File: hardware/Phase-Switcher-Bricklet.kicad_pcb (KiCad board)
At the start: 2 copper layers, 60 x 60 mm, 42 parts, among them CN1 HC-GH-7PWTKK, P1 WJ124-3.81-2P, P2 WJ124-3.81-6P, P3 WJ124-3.81-6P, U1 XMC1302-Q024X0032-AB, U2 AQY282SX, U3 AQH3213A, U4 HCPL2731S, U5 AQH3213A, U6 HCPL2731S

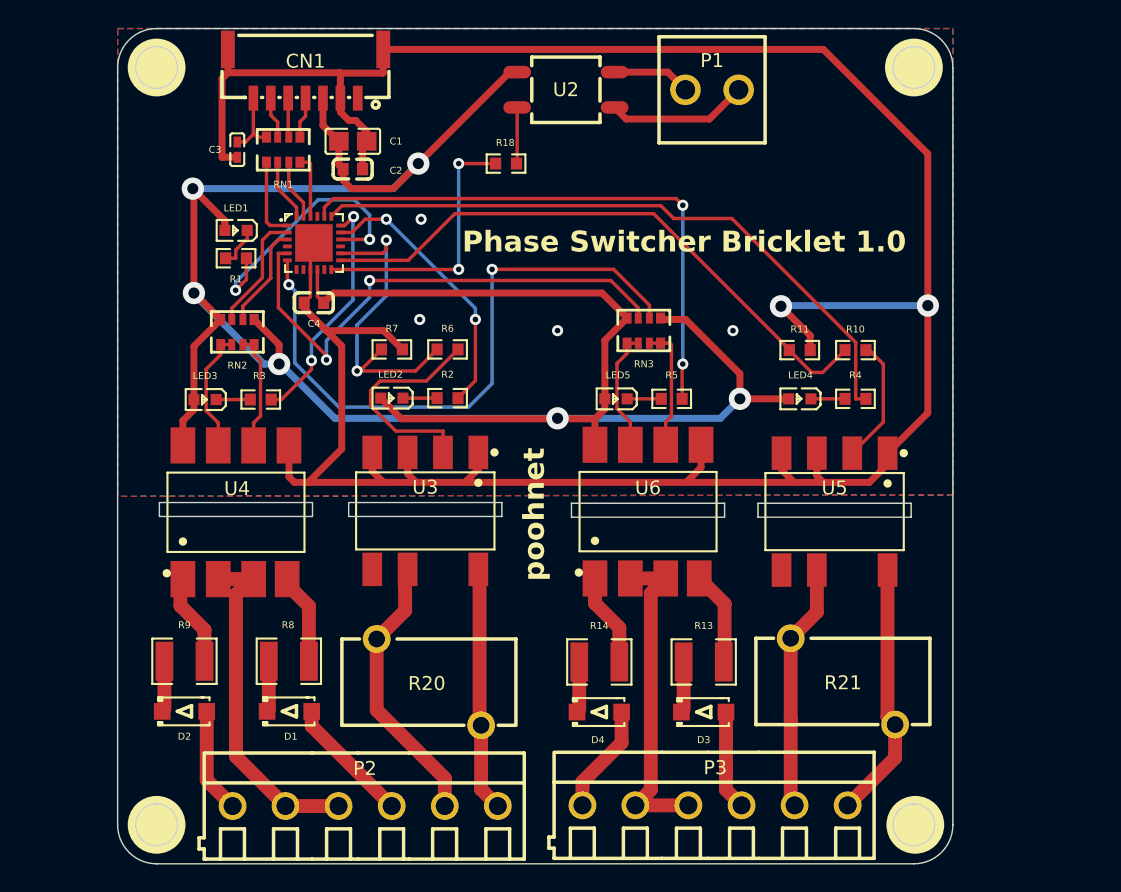
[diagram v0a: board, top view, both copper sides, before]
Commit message: Phase-Switcher-Bricklet: Rev. 1.1
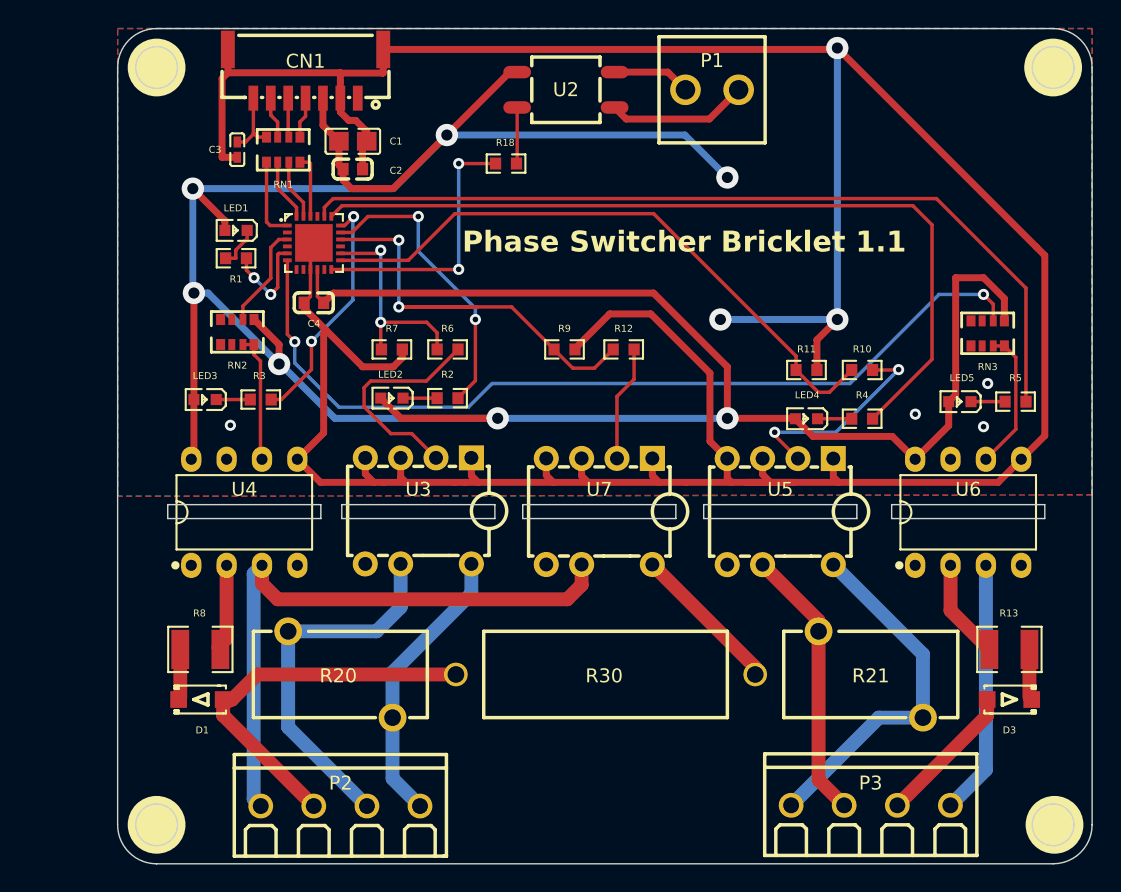
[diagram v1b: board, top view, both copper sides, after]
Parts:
- removed D2, D4: 1N4007, easyeda2kicad:SOD-123FL_L2.8-W1.8-LS3.7-RD
- removed R14: CR1210F249KP05, easyeda2kicad:R1210
- added R12: 150, easyeda2kicad:R0603, F.Cu at (92.8, 60.6)
- added R30: RSF5SSJR-73-4K7, easyeda2kicad:RES-TH_BD6.5-L17.5-P21.50-D0.6, F.Cu at (91.5, 84.0)
- added U7: AQH2213, easyeda2kicad:DIP-8_7P-L9.7-W6.4-P2.54-LS7.6-BL-PE7, F.Cu at (91.0, 72.3)
- P2, P3: value WJ124-3.81-6P -> WJ124-3.81-4P; footprint easyeda2kicad:CONN-TH_6P-P3.81_WJ124-3.81-6P -> easyeda2kicad:CONN-TH_4P-P3.81_KF124-3.81-4P
- R9: value CR1210F249KP05 -> 1K; footprint easyeda2kicad:R1210 -> easyeda2kicad:R0603
- U3, U5: value AQH3213A -> AQH2213; footprint easyeda2kicad:SMD-8_7P-L9.8-W6.4-P2.54-BL-PE7 -> easyeda2kicad:DIP-8_7P-L9.7-W6.4-P2.54-LS7.6-BL-PE7
- U4, U6: value HCPL2731S -> 6N139M; footprint easyeda2kicad:SMD-8_L9.8-W6.6-P2.54-LS10.3-BL -> easyeda2kicad:DIP-8_L9.4-W6.4-P2.54-LS9.1-BL
- moved R9 35.3 mm to (88.5, 60.6), turned to 0 degrees
- moved LED5 24.7 mm to (116.9, 64.4)
- moved R5 24.7 mm to (120.9, 64.4)
- moved RN3 24.7 mm to (118.9, 59.5)
- moved U6 23.0 mm to (117.5, 72.3)
- moved D3 22.0 mm to (120.5, 85.8), turned to 180 degrees
- moved R13 22.0 mm to (120.5, 82.2), turned to 0 degrees
- moved P3 11.2 mm to (110.5, 93.4)
- moved R8 6.42 mm to (62.3, 82.2)
- moved D1 6.42 mm to (62.4, 85.8)
- moved R20 6.38 mm to (72.4, 84.0)
- moved U5 3.90 mm to (104.0, 72.3)
- moved R21 2.06 mm to (110.5, 84.0)
- moved P2 1.78 mm to (72.4, 93.5)
- moved LED4 1.51 mm to (105.9, 65.6)
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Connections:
- net AC1-1 renamed AC1
- net AC2-1 renamed AC2
- P2 pad 4: Net-(U4-VF1-) -> Net-(U4-VF-)
- P3 pad 1: Net-(P3-Pad1) -> Net-(U6-VF-)
- P3 pad 2: Net-(P3-Pad2) -> Net-(D3-A)
- P3 pad 3: Net-(D3-A) -> Net-(P3-Pad3)
- P3 pad 4: Net-(U6-VF1-) -> Net-(P3-Pad4)
- R13 pad 1: Net-(U6-VF2+) -> Net-(U6-VF+)
- R21 pad 1: Net-(P3-Pad2) -> Net-(P3-Pad3)
- R21 pad 2: Net-(P3-Pad1) -> Net-(P3-Pad4)
- R8 pad 1: Net-(U4-VF2+) -> Net-(U4-VF+)
- R9 pad 1: Net-(U4-VF1+) -> RCD
- R9 pad 2: Net-(D2-K) -> GND
- RN2 pad 1: Net-(U4-VO1) -> unconnected-(RN2-Pad1)
- RN2 pad 2: Net-(U4-VO1) -> unconnected-(RN2-Pad2)
- RN2 pad 7: AC1-2 -> unconnected-(RN2-Pad7)
- RN2 pad 8: 3V3 -> unconnected-(RN2-Pad8)
- RN3 pad 1: Net-(U6-VO1) -> unconnected-(RN3-Pad1)
- RN3 pad 2: Net-(U6-VO1) -> unconnected-(RN3-Pad2)
- RN3 pad 7: AC2-2 -> unconnected-(RN3-Pad7)
- RN3 pad 8: 3V3 -> unconnected-(RN3-Pad8)
- U1 pad 16: LED1 -> RCD
- U1 pad 2: AC1-2 -> unconnected-(U1-P2.1-Pad2)
- U1 pad 5: AC2-2 -> LED1
- U4 pad 1: Net-(U4-VF1+) -> unconnected-(U4-N/C-Pad1)
- U4 pad 2: Net-(U4-VF1-) -> Net-(U4-VF+)
- U4 pad 3: Net-(U4-VF1-) -> Net-(U4-VF-)
- U4 pad 4: Net-(U4-VF2+) -> unconnected-(U4-N/C-Pad4)
- U4 pad 7: Net-(U4-VO1) -> unconnected-(U4-VB-Pad7)
- U5 pad 6: Net-(P3-Pad2) -> Net-(P3-Pad3)
- U5 pad 8: Net-(P3-Pad1) -> Net-(P3-Pad4)
- U6 pad 1: Net-(U6-VF1+) -> unconnected-(U6-N/C-Pad1)
- U6 pad 2: Net-(U6-VF1-) -> Net-(U6-VF+)
- U6 pad 3: Net-(U6-VF1-) -> Net-(U6-VF-)
- U6 pad 4: Net-(U6-VF2+) -> unconnected-(U6-N/C-Pad4)
- U6 pad 7: Net-(U6-VO1) -> unconnected-(U6-VB-Pad7)
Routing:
- net GND: track 198.1 -> 250.1 mm, vias 6 -> 7
- net Net-(U4-VF-): track 0.00 -> 44.4 mm
- net 3V3: track 175.9 -> 215.3 mm, vias 6 -> 7
- net AC2-2: track 37.5 -> 0.00 mm, vias 2 -> 0
- net RCD: track 0.00 -> 32.4 mm, vias 0 -> 2
- net Net-(U4-VF1-): track 25.9 -> 0.00 mm
- net Net-(P3-Pad4): track 0.00 -> 25.7 mm
- net Net-(P3-Pad2): track 23.7 -> 0.00 mm
- net Net-(U6-VF1-): track 23.6 -> 0.00 mm
- net LED5: track 40.8 -> 62.1 mm, vias 2 -> 0
- net Net-(P3-Pad3): track 0.00 -> 19.7 mm
- net Net-(D1-A): track 9.18 -> 27.8 mm
- net AC2: track 45.3 -> 63.9 mm
- net Net-(P3-Pad1): track 18.5 -> 0.00 mm
- net Net-(U6-VF-): track 0.00 -> 18.3 mm
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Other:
- board size 60 x 60 mm -> 70 x 60 mm
- board text added: "Phase Switcher Bricklet 1.1"
- board text removed: "Phase Switcher Bricklet 1.0"
- board text removed: "poohnet"

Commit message: Phase-Switcher-Bricklet: Rev. 1.1a
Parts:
- removed RN3: 10K, easyeda2kicad:RES-ARRAY-SMD_0603-8P-L3.2-W1.6-BL
- added LED6: blue, easyeda2kicad:LED0603-RD, F.Cu at (102.2, 58.4)
- added R6: 1K, easyeda2kicad:R0603, F.Cu at (105.9, 58.4)
- U10: renamed from U3; value AQH2213 -> AQH2223
- U20: renamed from U5; value AQH2213 -> AQH2223
- U30: renamed from U7; value AQH2213 -> AQH2223
- moved RN2 26.5 mm to (91.4, 61.6)
- moved U40 25.5 mm to (104.1, 62.2)
- moved P40 20.8 mm to (114.9, 55.5)
- moved R40 20.3 mm to (96.5, 63.5)
- moved C1 17.8 mm to (82.5, 61.0)
- moved C2 17.8 mm to (82.5, 63.0)
- moved CN1 16.0 mm to (78.0, 54.6)
- moved R11 15.2 mm to (65.5, 64.8)
- moved R10 15.0 mm to (61.7, 64.8), turned to 180 degrees
- moved R2 14.9 mm to (65.5, 67.3)
- moved LED2 14.8 mm to (61.7, 67.3)
- moved U20 14.2 mm to (118.1, 74.0)
- moved U10 14.1 mm to (64.0, 74.0)
- moved RN1 13.7 mm to (71.1, 59.7), turned to 90 degrees
- moved LED3 13.7 mm to (76.0, 67.3)
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- renumbered D1 to D10, D3 to D20, P2 to P10, P3 to P20, P1 to P40, R7 to R10, R6 to R11, R20 to R12, R8 to R13, R11 to R20, R10 to R21, R21 to R22, R13 to R23, R9 to R30, R12 to R31, R30 to R32, R18 to R40, U4 to U11, U6 to U21, U2 to U40
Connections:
- net Net-(U4-VO) renamed AC1-1
- D10 pad 2: Net-(D1-A) -> Net-(D10-A)
- D20 pad 2: Net-(D3-A) -> Net-(D20-A)
- P10 pad 1: Net-(P2-Pad1) -> Net-(U11-VF-)
- P10 pad 2: Net-(P2-Pad2) -> Net-(D10-A)
- P10 pad 3: Net-(D1-A) -> Net-(P10-Pad3)
- P10 pad 4: Net-(U4-VF-) -> Net-(P10-Pad4)
- P20 pad 1: Net-(U6-VF-) -> Net-(P20-Pad1)
- P20 pad 2: Net-(D3-A) -> Net-(P20-Pad2)
- P20 pad 3: Net-(P3-Pad3) -> Net-(D20-A)
- P20 pad 4: Net-(P3-Pad4) -> Net-(U21-VF-)
- R12 pad 1: Net-(P2-Pad2) -> Net-(P10-Pad4)
- R12 pad 2: Net-(P2-Pad1) -> Net-(P10-Pad3)
- R22 pad 1: Net-(P3-Pad3) -> Net-(P20-Pad2)
- R22 pad 2: Net-(P3-Pad4) -> Net-(P20-Pad1)
- R32 pad 2: Net-(D1-A) -> Net-(D10-A)
- RN2 pad 1: unconnected-(RN2-Pad1) -> AC2-1
- RN2 pad 2: unconnected-(RN2-Pad2) -> AC2-1
- RN2 pad 7: unconnected-(RN2-Pad7) -> 3V3
- RN2 pad 8: unconnected-(RN2-Pad8) -> AC2
- U1 pad 11: unconnected-(U1-P1.3-Pad11) -> RCD
- U1 pad 16: RCD -> LED1
- U1 pad 21: unconnected-(U1-P0.12-Pad21) -> LED6
- U1 pad 5: LED1 -> unconnected-(U1-P2.7/P2.8-Pad5)
- U10 pad 6: Net-(P2-Pad2) -> Net-(P10-Pad4)
- U10 pad 8: Net-(P2-Pad1) -> Net-(P10-Pad3)
- U11 pad 3: Net-(U4-VF-) -> Net-(U11-VF-)
- U20 pad 6: Net-(P3-Pad3) -> Net-(P20-Pad2)
- U20 pad 8: Net-(P3-Pad4) -> Net-(P20-Pad1)
- U21 pad 3: Net-(U6-VF-) -> Net-(U21-VF-)
- U21 pad 6: Net-(U6-VO) -> AC2-1
- U30 pad 6: Net-(U4-VF-) -> Net-(U11-VF-)
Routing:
- net GND: track 250.1 -> 128.8 mm, vias 7 -> 8
- net 3V3: track 215.3 -> 112.2 mm, vias 7 -> 0
- net RCD: track 32.4 -> 96.7 mm
- net LED6: track 0.00 -> 46.3 mm, vias 0 -> 2
- net Net-(U4-VF-): track 44.4 -> 0.00 mm
- net Net-(U11-VF-): track 0.00 -> 40.0 mm
- net AC2: track 63.9 -> 31.1 mm
- net Net-(D1-A): track 27.8 -> 0.00 mm
- net Net-(P2-Pad2): track 27.1 -> 0.00 mm
- net Net-(P3-Pad4): track 25.7 -> 0.00 mm
- net AC1: track 7.43 -> 32.2 mm, vias 0 -> 2
- net Net-(P20-Pad1): track 0.00 -> 22.3 mm
- net Net-(P10-Pad4): track 0.00 -> 22.1 mm
- net Net-(P2-Pad1): track 21.4 -> 0.00 mm
- net Net-(P20-Pad2): track 0.00 -> 20.8 mm
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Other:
- board size 70 x 60 mm -> 70 x 46.4 mm
- board text added: "poohnet"

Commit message: Phase-Switcher-Bricklet: Rev. 1.2
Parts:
- removed P20: WJ124-3.81-4P, easyeda2kicad:CONN-TH_4P-P3.81_KF124-3.81-4P
- removed R30: 1K, easyeda2kicad:R0603
- removed R31: 150, easyeda2kicad:R0603
- removed R32: RSF5SSJR-73-4K7, easyeda2kicad:RES-TH_BD6.5-L17.5-P21.50-D0.6
- removed U30: AQH2223, easyeda2kicad:DIP-8_7P-L9.7-W6.4-P2.54-LS7.6-BL-PE7
- added P11: WJ124-3.81-2P, easyeda2kicad:CONN-TH_2P-P3.81_KF124-3.81-2P, F.Cu at (87.0, 85.0)
- added P12: WJ124-3.81-2P, easyeda2kicad:CONN-TH_2P-P3.81_KF124-3.81-2P, F.Cu at (98.0, 85.0)
- moved U20 46.2 mm to (73.0, 64.0)
- moved R20 44.8 mm to (71.2, 54.0), turned to 180 degrees
- moved R21 44.8 mm to (75.2, 54.0)
- moved R22 44.6 mm to (74.0, 75.0)
- moved U40 23.6 mm to (88.0, 45.0)
- moved R40 23.2 mm to (81.0, 46.2)
- moved P40 19.9 mm to (98.0, 45.0)
- moved LED4 19.2 mm to (86.0, 57.0)
- moved R4 19.2 mm to (90.0, 57.0)
- moved LED5 17.9 mm to (100.0, 57.0)
- moved R5 17.9 mm to (104.0, 57.0)
- moved R13 15.1 mm to (87.0, 72.5), turned to 0 degrees
- moved C1 14.7 mm to (74.0, 49.0)
- moved C2 14.7 mm to (74.0, 51.0)
- moved D10 14.4 mm to (87.0, 77.0), turned to 180 degrees
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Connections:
- net AC1-1 renamed Net-(U11-VO)
- net AC2-1 renamed Net-(U21-VO)
- P10 pad 1: Net-(U11-VF-) -> Net-(P10-Pad1)
- P10 pad 2: Net-(D10-A) -> Net-(P10-Pad2)
- P10 pad 3: Net-(P10-Pad3) -> unconnected-(P10-Pad3)
- R12 pad 2: Net-(P10-Pad3) -> Net-(P10-Pad2)
- R22 pad 1: Net-(P20-Pad2) -> Net-(P10-Pad2)
- R22 pad 2: Net-(P20-Pad1) -> Net-(P10-Pad1)
- U1 pad 11: RCD -> unconnected-(U1-P1.3-Pad11)
- U1 pad 12: CP -> unconnected-(U1-P1.2-Pad12)
- U1 pad 15: unconnected-(U1-P0.0-Pad15) -> CP
- U10 pad 8: Net-(P10-Pad3) -> Net-(P10-Pad2)
- U20 pad 6: Net-(P20-Pad2) -> Net-(P10-Pad2)
- U20 pad 8: Net-(P20-Pad1) -> Net-(P10-Pad1)
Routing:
- net GND: track 128.8 -> 15.0 mm
- net RCD: track 96.7 -> 0.00 mm, vias 2 -> 0
- net 3V3: track 112.2 -> 150.6 mm
- net Net-(P10-Pad2): track 0.00 -> 34.6 mm
- net Relay2: track 61.0 -> 29.3 mm, vias 4 -> 0
- net Net-(U11-VF-): track 40.0 -> 17.3 mm
- net Net-(P20-Pad1): track 22.3 -> 0.00 mm
- net Net-(P20-Pad2): track 20.8 -> 0.00 mm
- net Net-(P10-Pad3): track 20.3 -> 0.00 mm
- net Net-(P10-Pad1): track 0.00 -> 20.1 mm
- net Net-(R32-Pad1): track 11.5 -> 0.00 mm
- net LED1: track 25.0 -> 13.5 mm
- net LED4: track 44.9 -> 35.0 mm, vias 2 -> 0
- net Net-(U11-VO): track 19.7 -> 10.4 mm
- net LED5: track 57.6 -> 48.8 mm, vias 2 -> 0
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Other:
- board size 70 x 46.4 mm -> 60 x 50 mm
- board text added: "Phase Switcher Bricklet 1.2"
- board text removed: "Phase Switcher Bricklet 1.1"

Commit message: Phase-Switcher-Bricklet: Rev. 1.3
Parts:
- R13, R23: value CR1210F249KP05 -> RN1/2WS249KΩFT/BA1; footprint easyeda2kicad:R1210 -> easyeda2kicad:RES-TH_BD2.2-L6.5-P10.50-D0.6
- moved R13 6.73 mm to (82.0, 77.0), turned to 90 degrees
- moved R23 6.05 mm to (94.0, 77.0), turned to 90 degrees
- moved D20 1.03 mm to (99.0, 76.8)
- moved P21 1.00 mm to (99.0, 85.0)
- moved R12 1.00 mm to (58.0, 75.0)
- moved R22 1.00 mm to (73.0, 75.0)
- moved D10 0.25 mm to (87.0, 76.8), turned to 0 degrees
- renumbered P12 to P21, P40 to P30, R40 to R30, U40 to U30
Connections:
- R13 pad 1: Net-(U11-VF+) -> Net-(D10-K)
- R13 pad 2: Net-(D10-K) -> Net-(U11-VF+)
- R23 pad 1: Net-(U21-VF+) -> Net-(D20-K)
- R23 pad 2: Net-(D20-K) -> Net-(U21-VF+)
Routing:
- net 3V3: track 150.6 -> 169.0 mm
- net Net-(U21-VF+): track 5.22 -> 9.27 mm
- net Net-(P10-Pad2): track 34.6 -> 37.5 mm
- net Net-(D20-K): track 4.57 -> 6.93 mm
- net Net-(D10-K): track 4.57 -> 6.91 mm
- net GND: track 15.0 -> 17.1 mm
- net Net-(U11-VF+): track 5.40 -> 7.22 mm
- net Net-(D10-A): track 8.13 -> 9.70 mm
- net LED1: track 13.5 -> 12.6 mm
- net Net-(P10-Pad1): track 20.1 -> 19.3 mm
- net Net-(P10-Pad4): track 20.1 -> 20.7 mm
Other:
- outline, holes or cut-outs redrawn
- board text added: "Phase Switcher Bricklet 1.3"
- board text removed: "Phase Switcher Bricklet 1.2"
